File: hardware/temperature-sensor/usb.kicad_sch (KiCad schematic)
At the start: 20 parts, among them J2 AMPHENOL_micro_usb_10118194-0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, U3 FT230XS

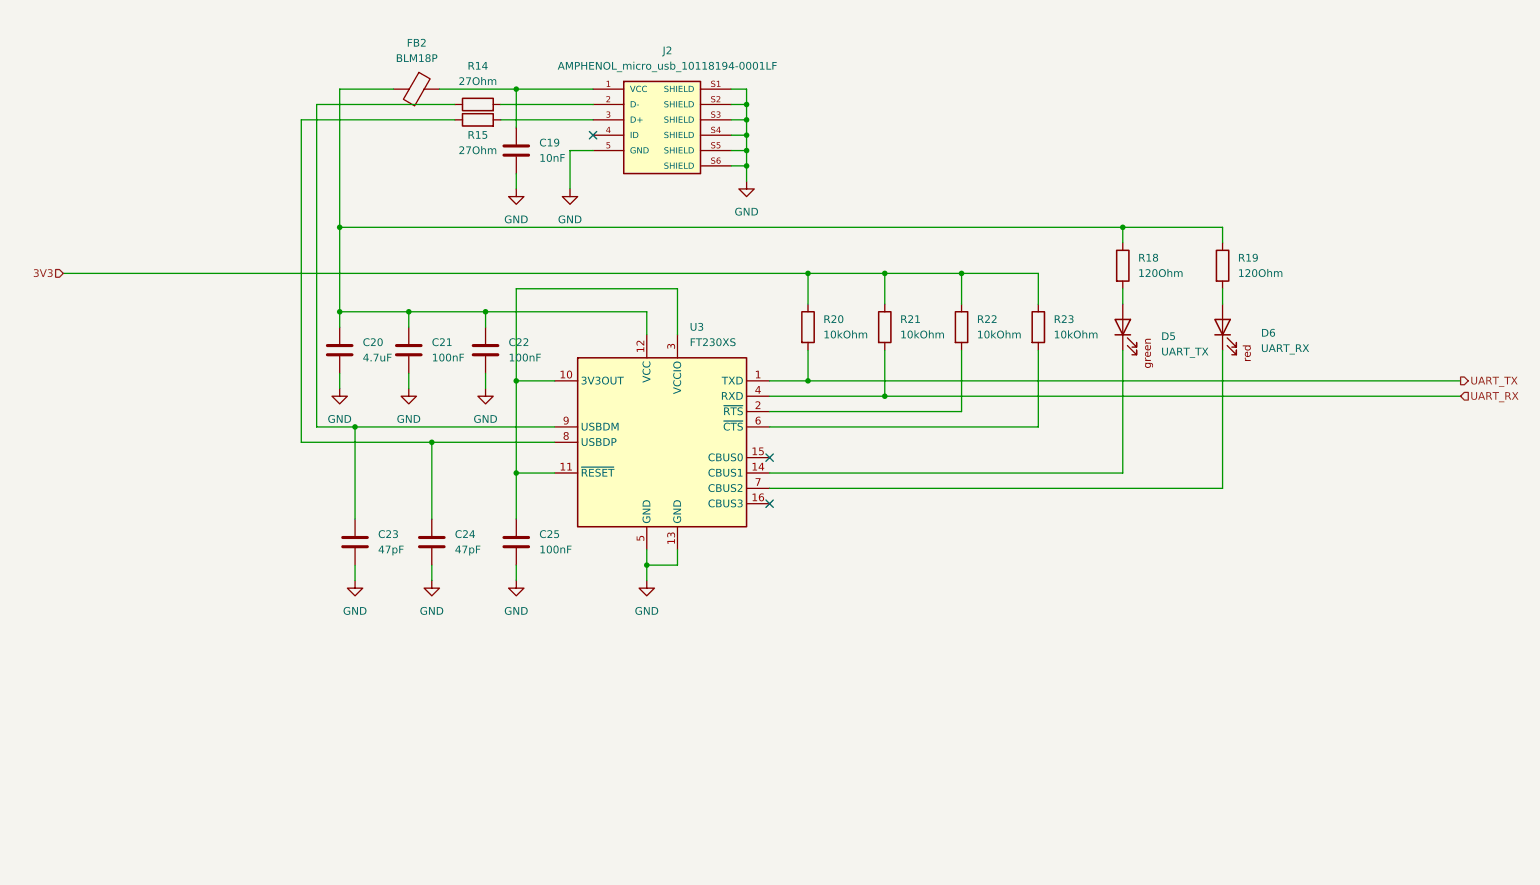
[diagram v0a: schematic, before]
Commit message: replace USB micro with USB c
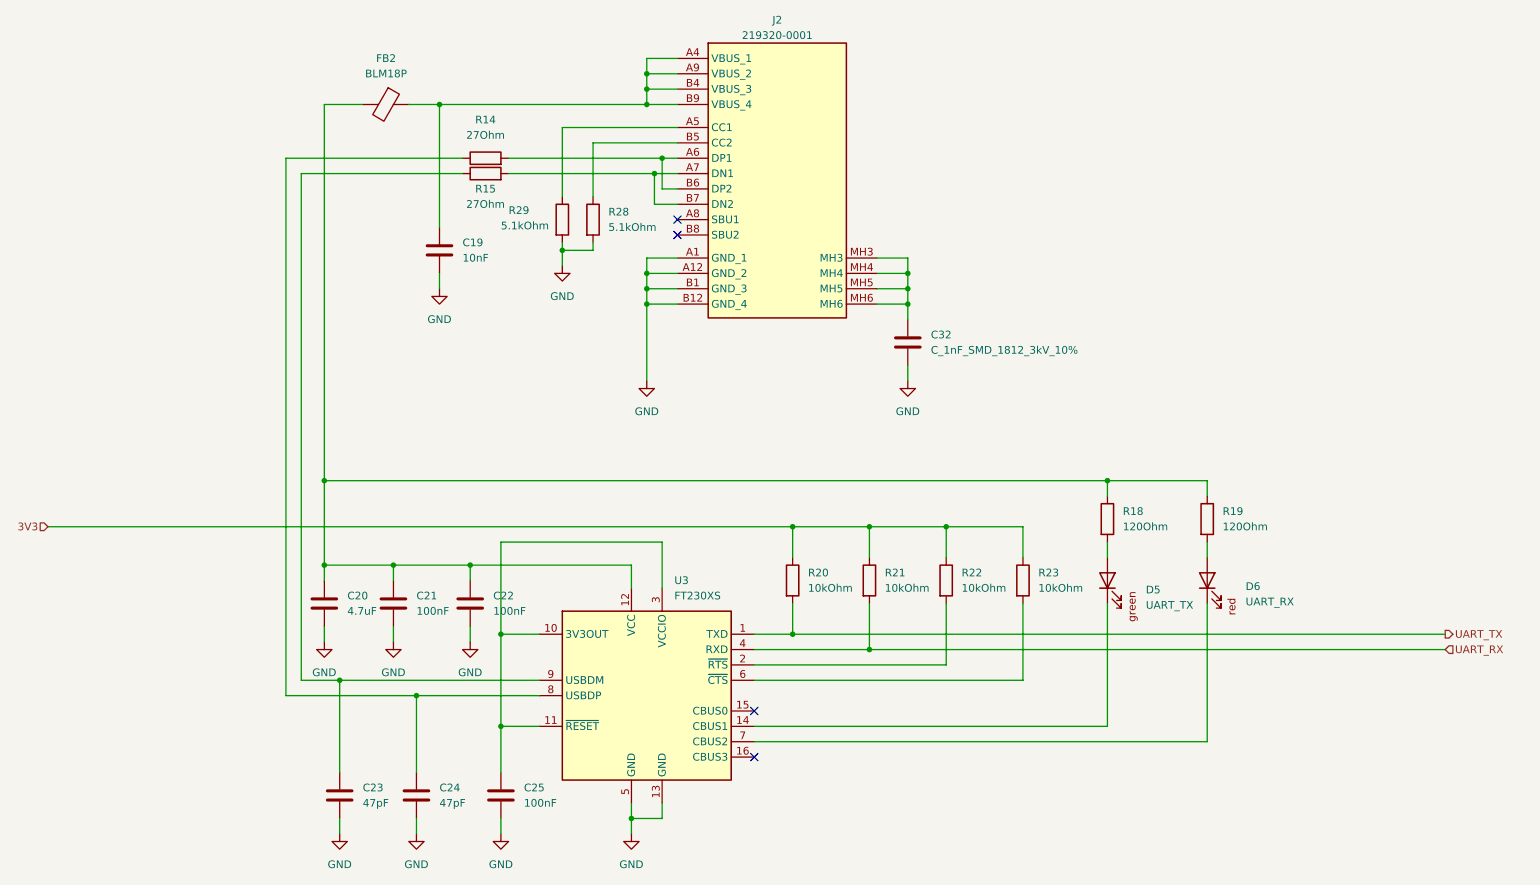
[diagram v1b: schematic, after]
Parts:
- removed J2: AMPHENOL_micro_usb_10118194-0001LF, benediktibk:AMPHENOL_10118194-0001LF, symbol benediktibk:AMPHENOL_micro_usb_10118194-0001LF
- added C32: C_1nF_SMD_1812_3kV_10%, benediktibk:C_0603_1608Metric_Pad1.08x0.95mm_HandSolder, symbol benediktibk:C_1nF_SMD_1812_3kV_10%
- added J2: 219320-0001, benediktibk:2193200001, symbol benediktibk:219320-0001
- added R28, R29: 5.1kOhm, benediktibk:R_0603_1608Metric_Pad0.98x0.95mm_HandSolder, symbol benediktibk:R_5_1kOhm_SMD_0603_100mW_1%
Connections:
- net GND: now also C32.2, J2.A1 (GND_1), J2.A12 (GND_2), J2.B1 (GND_3), J2.B12 (GND_4), R28.2, R29.2
- net at C19.1, FB2.1: now also J2.A4 (VBUS_1), J2.A9 (VBUS_2), J2.B4 (VBUS_3), J2.B9 (VBUS_4)
- net at R14.2: now also J2.A6 (DP1), J2.B6 (DP2)
- net at R15.2: now also J2.A7 (DN1), J2.B7 (DN2)
- net at C24.1, U3.8 (USBDP): now also R14.1; no longer R15.1
- net at C23.1, U3.9 (USBDM): now also R15.1; no longer R14.1
- new net: J2.A5 (CC1), R29.1
- new net: J2.B5 (CC2), R28.1
- new net: C32.1, J2.MH3, J2.MH4, J2.MH5, J2.MH6
- no-connect marks 3 -> 4
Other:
- moved on the sheet: C19, C20, C21, C22, C23, C24, C25, D5, D6, FB2, R14, R15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
